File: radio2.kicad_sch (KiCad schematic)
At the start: 18 parts, among them U4 CC1125RHBR, Y1 OW7EL89CENUYO3YLC-40M

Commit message: Finish up inputting things
Signed-off-by: Corey Minyard <corey@minyard.net>
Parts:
- added C49: 39pF, Capacitor_SMD:C_0402_1005Metric_Pad0.74x0.62mm_HandSolder, symbol Device:C
- added C53: 56pF, Capacitor_SMD:C_0402_1005Metric_Pad0.74x0.62mm_HandSolder, symbol Device:C
- added L18: 56nH, Inductor_SMD:L_1210_3225Metric_Pad1.42x2.65mm_HandSolder, symbol Device:L
- added R16: 18, Resistor_SMD:R_0402_1005Metric, symbol Device:R
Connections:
- net 440_TX: now also C49.2; no longer U4.17 (PA)
- new net: C53.1, L18.2, R16.1
- new net: C49.1, L18.1, U4.17 (PA)
- new net +5V: C53.2, R16.2
- no-connect marks 3 -> 5

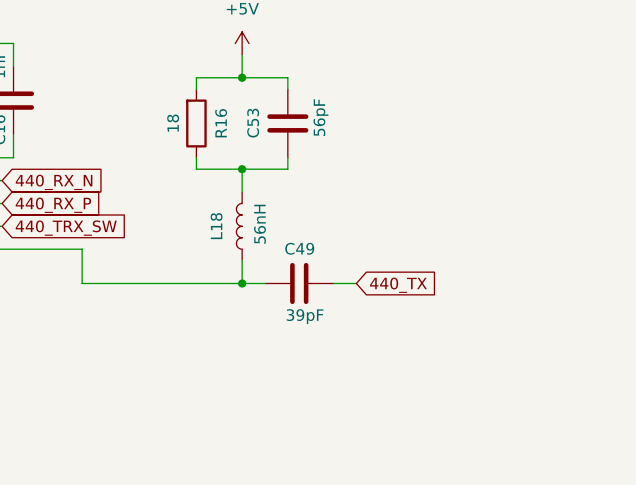
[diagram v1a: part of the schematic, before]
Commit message: Clean up schematics
Signed-off-by: Corey Minyard <corey@minyard.net>
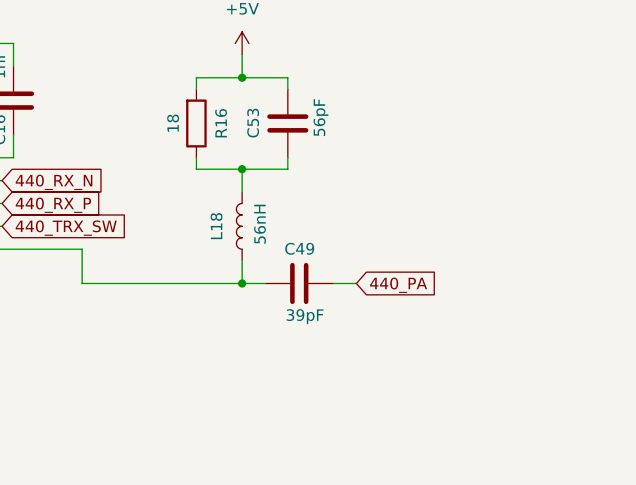
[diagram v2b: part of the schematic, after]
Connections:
- net 440_TX renamed 440_PA
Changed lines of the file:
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@@
 		)
 	)
-	(global_label "440_TX"
+	(global_label "440_PA"
 		(shape input)
 		(at 227.33 119.38 0)
@@
 		)
 		(property "Intersheetrefs" "${INTERSHEET_REFS}"
-			(at 237.0884 119.38 0)
+			(at 237.2699 119.38 0)
 			(effects
 				(font
@@
 		(pin "8"
 		)
-	)
+		(instances
+			(project ""
+				(path "/23e49ab9-97e0-460a-806c-ff6f37958474/cf3ac92b-a340-4acf-be56-0f2a6ee7b165"
+					(reference "U4")
+					(unit 1)
+				)
+			)
+		)
+	)

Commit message: More cleanups and add some test points
Signed-off-by: Corey Minyard <corey@minyard.net>
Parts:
- L18: footprint Inductor_SMD:L_1210_3225Metric_Pad1.42x2.65mm_HandSolder -> Inductor_SMD:L_0603_1608Metric_Pad1.05x0.95mm_HandSolder
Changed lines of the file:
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@@
 			)
 		)
-		(property "Footprint" "Inductor_SMD:L_1210_3225Metric_Pad1.42x2.65mm_HandSolder"
+		(property "Footprint" "Inductor_SMD:L_0603_1608Metric_Pad1.05x0.95mm_HandSolder"
 			(at 214.63 113.03 0)
 			(effects

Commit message: Finish layout
Signed-off-by: Corey Minyard <corey@minyard.net>
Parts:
- C14, C17, C18, C19, C20, C21, C22, C23, C24, C25, C26, C27, C28: footprint Capacitor_SMD:C_0603_1608Metric_Pad1.08x0.95mm_HandSolder -> Capacitor_SMD:C_0402_1005Metric_Pad0.74x0.62mm_HandSolder

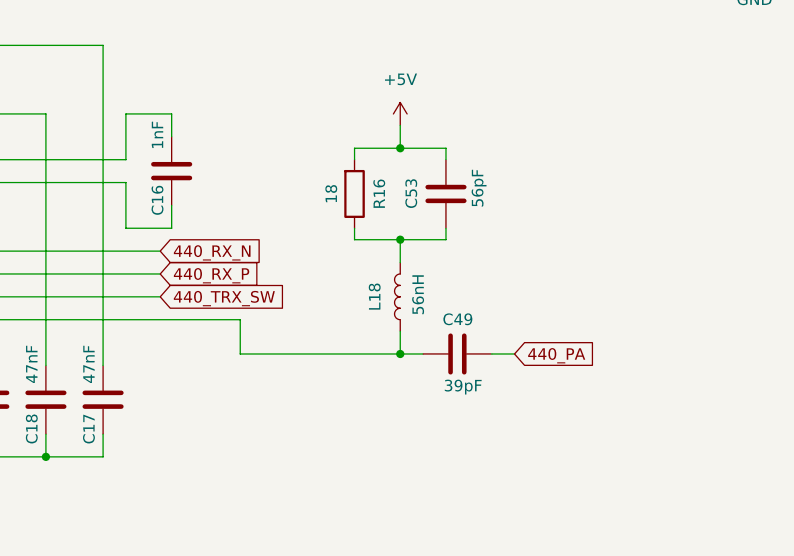
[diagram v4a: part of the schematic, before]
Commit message: Start working on BOM, fix supply indoctors
Signed-off-by: Corey Minyard <corey@minyard.net>
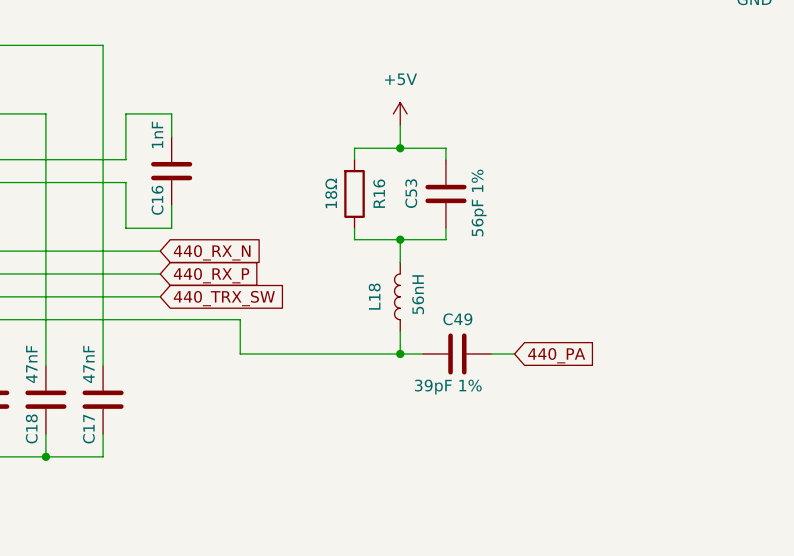
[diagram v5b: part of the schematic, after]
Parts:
- C16: footprint Capacitor_SMD:C_0603_1608Metric_Pad1.08x0.95mm_HandSolder -> Capacitor_SMD:C_0402_1005Metric_Pad0.74x0.62mm_HandSolder
- C49: value 39pF -> 39pF 1%
- C53: value 56pF -> 56pF 1%
- R16: value 18 -> 18Ω
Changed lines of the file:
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@@
 			)
 		)
-		(property "Value" "18"
+		(property "Value" "18Ω"
 			(at 207.01 101.6 90)
 			(effects
@@
 			)
 		)
-		(property "Value" "39pF"
+		(property "Value" "39pF 1%"
 			(at 223.774 122.936 90)
 			(effects
@@
 			)
 		)
-		(property "Value" "56pF"
+		(property "Value" "56pF 1%"
 			(at 223.266 98.806 90)
 			(effects
@@
 			)
 		)
-		(property "Footprint" "Capacitor_SMD:C_0603_1608Metric_Pad1.08x0.95mm_HandSolder"
+		(property "Footprint" "Capacitor_SMD:C_0402_1005Metric_Pad0.74x0.62mm_HandSolder"
 			(at 188.2648 95.25 0)
 			(effects

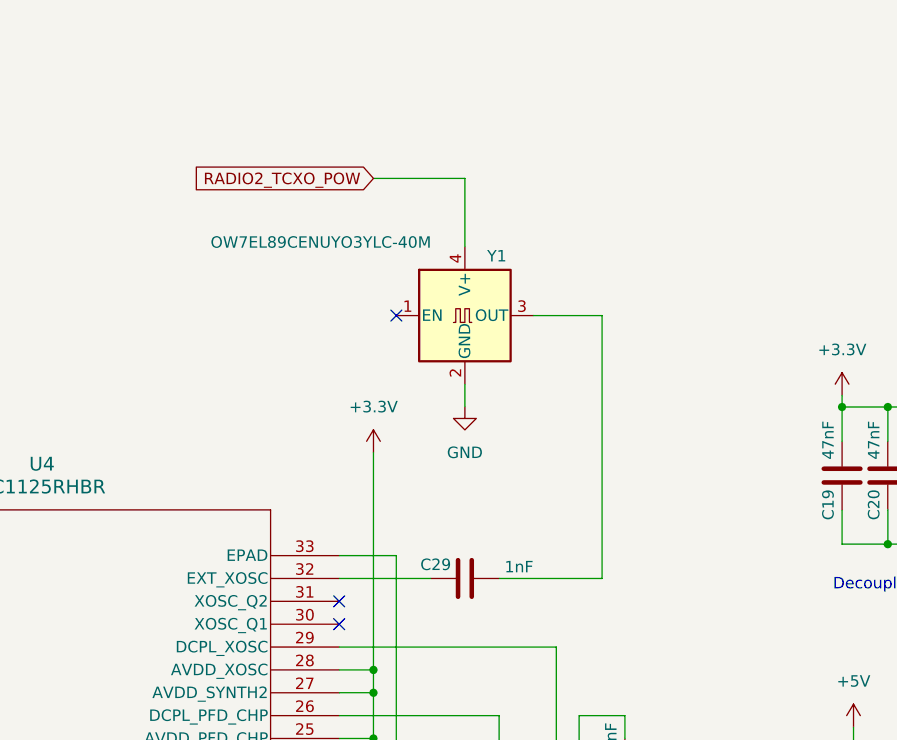
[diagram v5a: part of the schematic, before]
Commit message: Directly power the oscillators
There is only one D/A converter on the CC1312R, so you really couldn't
power both of the oscillators from that chip.  Power is not a concern,
so just directly power them from 3.3V.  That required using a different
oscillator chip, too, but it was available on both frequencies.

Signed-off-by: Corey Minyard <corey@minyard.net>
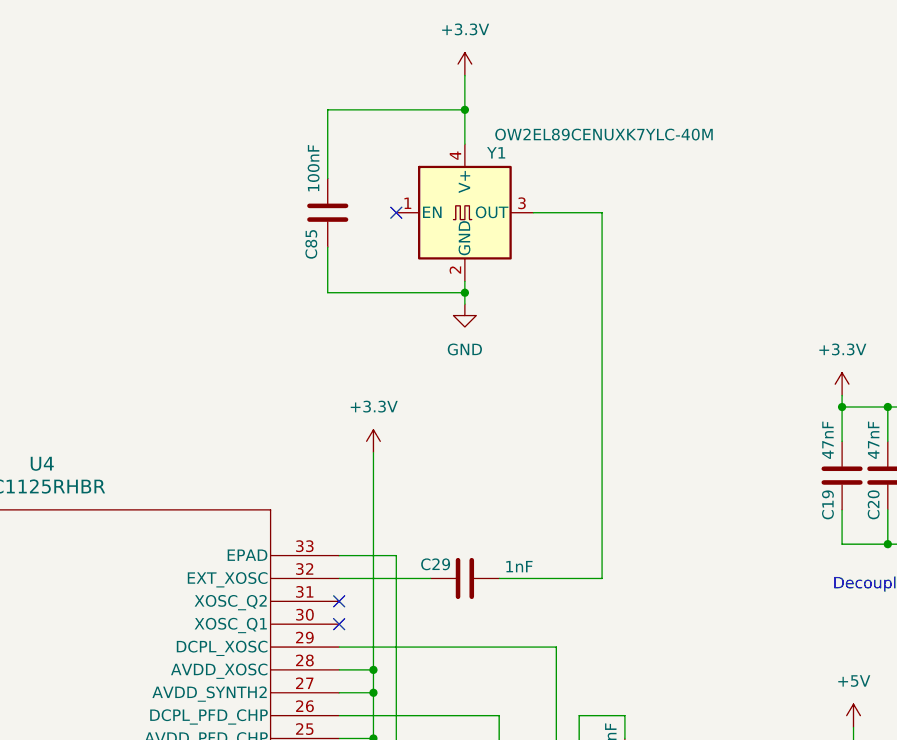
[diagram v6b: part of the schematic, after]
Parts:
- added C85: 100nF, Capacitor_SMD:C_0402_1005Metric_Pad0.74x0.62mm_HandSolder, symbol Device:C
- Y1: value OW7EL89CENUYO3YLC-40M -> OW2EL89CENUXK7YLC-40M
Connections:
- net RADIO2_TCXO_POW is gone; now on net +3.3V: Y1.4 (V+)
- net +3.3V: now also C85.2
- net GND: now also C85.1
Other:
- moved on the sheet: Y1
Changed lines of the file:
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@@
+	)
+	(junction
+		(at 171.45 25.4)
+		(diameter 0)
+		(color 0 0 0 0)
 	)
 	(junction
@@
 		(color 0 0 0 0)
 	)
+	(junction
+		(at 171.45 45.72)
+		(diameter 0)
+		(color 0 0 0 0)
+	)
 	(no_connect
 		(at 157.48 80.01)
@@
 	)
 	(no_connect
-		(at 163.83 48.26)
+		(at 163.83 36.83)
 	)
 	(no_connect
@@
 	(wire
 		(pts
+			(xy 171.45 25.4) (xy 171.45 29.21)
+		)
+		(stroke
+			(width 0)
+			(type default)
+		)
+	)
+	(wire
+		(pts
 			(xy 59.69 90.17) (xy 91.44 90.17)
 		)
@@
 	(wire
 		(pts
-			(xy 171.45 33.02) (xy 171.45 40.64)
+			(xy 171.45 21.59) (xy 171.45 25.4)
 		)
 		(stroke
@@
 	(wire
 		(pts
-			(xy 161.29 33.02) (xy 171.45 33.02)
-		)
-		(stroke
-			(width 0)
-			(type default)
-		)
-	)
-	(wire
-		(pts
 			(xy 243.84 58.42) (xy 248.92 58.42)
 		)
@@
 	(wire
 		(pts
-			(xy 186.69 48.26) (xy 179.07 48.26)
+			(xy 186.69 36.83) (xy 179.07 36.83)
 		)
 		(stroke
@@
 	(wire
 		(pts
-			(xy 171.45 55.88) (xy 171.45 58.42)
+			(xy 171.45 44.45) (xy 171.45 45.72)
 		)
 		(stroke
@@
 	(wire
 		(pts
+			(xy 171.45 45.72) (xy 171.45 46.99)
+		)
+		(stroke
+			(width 0)
+			(type default)
+		)
+	)
+	(wire
+		(pts
 			(xy 157.48 102.87) (xy 161.29 102.87)
 		)
@@
 	(wire
 		(pts
+			(xy 156.21 25.4) (xy 171.45 25.4)
+		)
+		(stroke
+			(width 0)
+			(type default)
+		)
+	)
+	(wire
+		(pts
 			(xy 218.44 58.42) (xy 213.36 58.42)
 		)
@@
 	(wire
 		(pts
-			(xy 186.69 77.47) (xy 186.69 48.26)
+			(xy 186.69 77.47) (xy 186.69 36.83)
 		)
 		(stroke
@@
 	(wire
 		(pts
+			(xy 156.21 45.72) (xy 171.45 45.72)
+		)
+		(stroke
+			(width 0)
+			(type default)
+		)
+	)
+	(wire
+		(pts
 			(xy 87.63 85.09) (xy 87.63 74.93)
 		)
@@
 	(wire
 		(pts
+			(xy 156.21 33.02) (xy 156.21 25.4)
+		)
+		(stroke
+			(width 0)
+			(type default)
+		)
+	)
+	(wire
+		(pts
+			(xy 156.21 40.64) (xy 156.21 45.72)
+		)
+		(stroke
+			(width 0)
+			(type default)
+		)
+	)
+	(wire
+		(pts
 			(xy 157.48 90.17) (xy 161.29 90.17)
 		)
@@
 			(width 0)
 			(type default)
-		)
-	)
-	(global_label "RADIO2_TCXO_POW"
-		(shape input)
-		(at 161.29 33.02 180)
-		(fields_autoplaced yes)
-		(effects
-			(font
-				(size 1.27 1.27)
-			)
-			(justify right)
-		)
-		(property "Intersheetrefs" "${INTERSHEET_REFS}"
-			(at 140.7667 33.02 0)
-			(effects
-				(font
-					(size 1.27 1.27)
-				)
-				(justify right)
-				(hide yes)
-			)
 		)
 	)
@@
 	)
 	(symbol
+		(lib_id "Device:C")
+		(at 156.21 36.83 180)
+		(unit 1)
+		(exclude_from_sim no)
+		(in_bom yes)
+		(on_board yes)
+		(dnp no)
+		(property "Reference" "C85"
+			(at 154.432 38.608 90)
+			(effects
+				(font
+					(size 1.27 1.27)
+				)
+				(justify left)
+			)
+		)
+		(property "Value" "100nF"
+			(at 154.686 29.21 90)
+			(effects
+				(font
+					(size 1.27 1.27)
+				)
+				(justify left)
+			)
+		)
+		(property "Footprint" "Capacitor_SMD:C_0402_1005Metric_Pad0.74x0.62mm_HandSolder"
+			(at 155.2448 33.02 0)
+			(effects
+				(font
+					(size 1.27 1.27)
+				)
+				(hide yes)
+			)
+		)
+		(property "Datasheet" "~"
+			(at 156.21 36.83 0)
+			(effects
+				(font
+					(size 1.27 1.27)
+				)
+				(hide yes)
+			)
+		)
+		(property "Description" "Unpolarized capacitor"
+			(at 156.21 36.83 0)
+			(effects
+				(font
+					(size 1.27 1.27)
+				)
+				(hide yes)
+			)
+		)
+		(pin "2"
+		)
+		(pin "1"
+		)
+		(instances
+			(project "FSKGroundStation"
+				(path "/23e49ab9-97e0-460a-806c-ff6f37958474/cf3ac92b-a340-4acf-be56-0f2a6ee7b165"
+					(reference "C85")
+					(unit 1)
+				)
+			)
+		)
+	)
+	(symbol
 		(lib_id "power:+3.3V")
 		(at 213.36 57.15 0)
@@
 	)
 	(symbol
+		(lib_id "power:+3.3V")
+		(at 171.45 21.59 0)
+		(unit 1)
+		(exclude_from_sim no)
+		(in_bom yes)
+		(on_board yes)
+		(dnp no)
+		(fields_autoplaced yes)
+		(property "Reference" "#PWR096"
+			(at 171.45 25.4 0)
+			(effects
+				(font
+					(size 1.27 1.27)
+				)
+				(hide yes)
+			)
+		)
+		(property "Value" "+3.3V"
+			(at 171.45 16.51 0)
+			(effects
+				(font
+					(size 1.27 1.27)
+				)
+			)
+		)
+		(property "Footprint" ""
+			(at 171.45 21.59 0)
+			(effects
+				(font
+					(size 1.27 1.27)
+				)
+				(hide yes)
+			)
+		)
+		(property "Datasheet" ""
+			(at 171.45 21.59 0)
+			(effects
+				(font
+					(size 1.27 1.27)
+				)
+				(hide yes)
+			)
+		)
+		(property "Description" "Power symbol creates a global label with name \"+3.3V\""
+			(at 171.45 21.59 0)
+			(effects
+				(font
+					(size 1.27 1.27)
+				)
+				(hide yes)
+			)
+		)
+		(pin "1"
+		)
+		(instances
+			(project "FSKGroundStation"
+				(path "/23e49ab9-97e0-460a-806c-ff6f37958474/cf3ac92b-a340-4acf-be56-0f2a6ee7b165"
+					(reference "#PWR096")
+					(unit 1)
+				)
+			)
+		)
+	)
+	(symbol
 		(lib_id "Device:C")
 		(at 223.52 66.04 180)
@@
 	(symbol
 		(lib_id "power:GND")
-		(at 171.45 58.42 0)
+		(at 171.45 46.99 0)
 		(unit 1)
 		(exclude_from_sim no)
@@
 		(fields_autoplaced yes)
 		(property "Reference" "#PWR031"
-			(at 171.45 64.77 0)
+			(at 171.45 53.34 0)
 			(effects
 				(font
@@
 		)
 		(property "Value" "GND"
-			(at 171.45 63.5 0)
+			(at 171.45 52.07 0)
 			(effects
 				(font
@@
 		)
 		(property "Footprint" ""
-			(at 171.45 58.42 0)
+			(at 171.45 46.99 0)
 			(effects
 				(font
@@
 		)
 		(property "Datasheet" ""
-			(at 171.45 58.42 0)
+			(at 171.45 46.99 0)
 			(effects
 				(font
@@
 		)
 		(property "Description" "Power symbol creates a global label with name \"GND\" , ground"
-			(at 171.45 58.42 0)
+			(at 171.45 46.99 0)
 			(effects
 				(font
@@
 	(symbol
 		(lib_id "Local Passives:TXCO")
-		(at 171.45 48.26 0)
+		(at 171.45 36.83 0)
 		(unit 1)
 		(exclude_from_sim no)
@@
 		(dnp no)
 		(property "Reference" "Y1"
-			(at 175.006 41.656 0)
-			(effects
-				(font
-					(size 1.27 1.27)
-				)
-			)
-		)
-		(property "Value" "OW7EL89CENUYO3YLC-40M"
-			(at 155.448 40.132 0)
+			(at 175.006 30.226 0)
+			(effects
+				(font
+					(size 1.27 1.27)
+				)
+			)
+		)
+		(property "Value" "OW2EL89CENUXK7YLC-40M"
+			(at 186.944 28.194 0)
 			(effects
 				(font
@@
 		)
 		(property "Footprint" "Oscillator:Oscillator_SMD_SiT_PQFN-4Pin_2.0x1.6mm"
-			(at 189.23 57.15 0)
+			(at 189.23 45.72 0)
 			(effects
 				(font
@@
 		)
 		(property "Datasheet" ""
-			(at 168.91 48.26 0)
+			(at 168.91 36.83 0)
 			(effects
 				(font
@@
 		)
 		(property "Description" "TXCO 2.0mmx1.6mm"
-			(at 171.45 48.26 0)
-			(effects
-				(font
+			(at 171.45 36.83 0)
+			(effects
+				(font

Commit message: Fix some oscillator issues
Ground an unused oscillator line on the CC1125 that needs to be grounded
in external oscillator mode.

Add a resistor divider to the oscillator inputs in case the voltage
needs to be decreased.  It should be fixable with the internal capacitor
tuning, but just in case.

Signed-off-by: Corey Minyard <corey@minyard.net>
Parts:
- added R14, R31: 0Ω, Resistor_SMD:R_0402_1005Metric, symbol Device:R
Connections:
- net GND: now also U4.30 (XOSC_Q1), R31.1
- net at Y1.3 (OUT): now also R14.2; no longer C29.2
- new net: C29.2, R14.1, R31.2
- no-connect marks 5 -> 4
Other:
- note added: "This is in case we need to reduce the voltage into the oscillator pin."

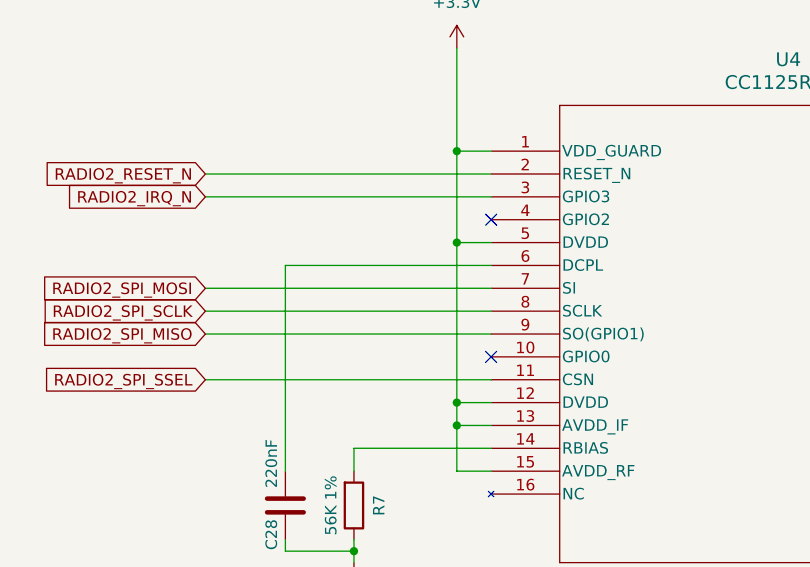
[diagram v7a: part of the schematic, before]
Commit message: Make a bunch of GPIOs more easily available
Put them on DNP zero-ohm resistors.

Signed-off-by: Corey Minyard <corey@minyard.net>
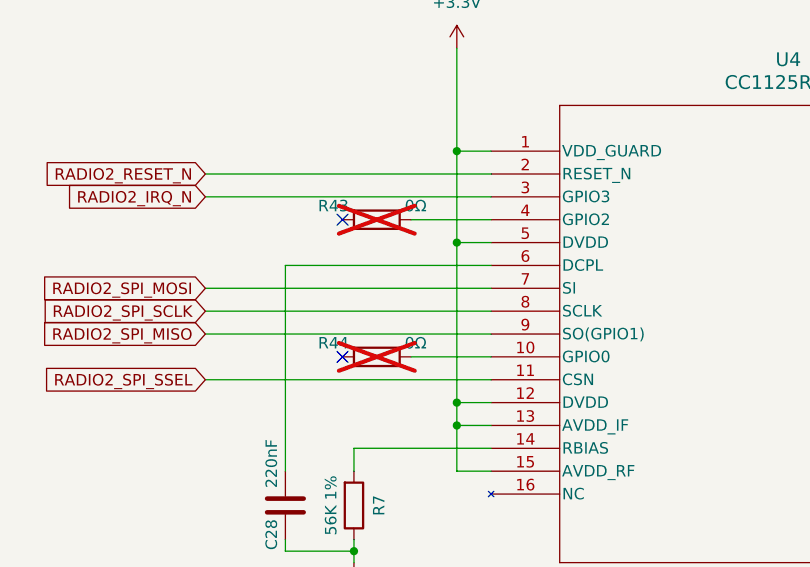
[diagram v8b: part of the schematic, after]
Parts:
- added R43, R44: 0Ω, Resistor_SMD:R_0402_1005Metric, symbol Device:R
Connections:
- net at U4.10 (GPIO0): now also R44.1
- net at U4.4 (GPIO2): now also R43.1
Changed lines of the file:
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@@
 	)
 	(no_connect
-		(at 91.44 97.79)
+		(at 74.93 82.55)
+	)
+	(no_connect
+		(at 74.93 97.79)
 	)
 	(no_connect
 		(at 163.83 36.83)
 	)
-	(no_connect
-		(at 91.44 82.55)
-	)
 	(wire
 		(pts
@@
 	(wire
 		(pts
+			(xy 82.55 97.79) (xy 91.44 97.79)
+		)
+		(stroke
+			(width 0)
+			(type default)
+		)
+	)
+	(wire
+		(pts
 			(xy 189.23 102.87) (xy 189.23 105.41)
 		)
@@
 		(pts
 			(xy 87.63 110.49) (xy 87.63 105.41)
+		)
+		(stroke
+			(width 0)
+			(type default)
+		)
+	)
+	(wire
+		(pts
+			(xy 82.55 82.55) (xy 91.44 82.55)
 		)
 		(stroke
@@
 	)
 	(symbol
+		(lib_id "Device:R")
+		(at 78.74 82.55 270)
+		(unit 1)
+		(exclude_from_sim no)
+		(in_bom no)
+		(on_board yes)
+		(dnp yes)
+		(property "Reference" "R43"
+			(at 73.914 81.026 90)
+			(effects
+				(font
+					(size 1.27 1.27)
+				)
+			)
+		)
+		(property "Value" "0Ω"
+			(at 83.058 81.026 90)
+			(effects
+				(font
+					(size 1.27 1.27)
+				)
+			)
+		)
+		(property "Footprint" "Resistor_SMD:R_0402_1005Metric"
+			(at 78.74 80.772 90)
+			(effects
+				(font
+					(size 1.27 1.27)
+				)
+				(hide yes)
+			)
+		)
+		(property "Datasheet" "~"
+			(at 78.74 82.55 0)
+			(effects
+				(font
+					(size 1.27 1.27)
+				)
+				(hide yes)
+			)
+		)
+		(property "Description" "Resistor"
+			(at 78.74 82.55 0)
+			(effects
+				(font
+					(size 1.27 1.27)
+				)
+				(hide yes)
+			)
+		)
+		(pin "2"
+		)
+		(pin "1"
+		)
+		(instances
+			(project "FSKGroundStation"
+				(path "/23e49ab9-97e0-460a-806c-ff6f37958474/cf3ac92b-a340-4acf-be56-0f2a6ee7b165"
+					(reference "R43")
+					(unit 1)
+				)
+			)
+		)
+	)
+	(symbol
 		(lib_id "power:GND")
 		(at 191.77 59.69 0)
@@
 					(unit 1)
 				)
+			)
+		)
+	)
+	(symbol
+		(lib_id "Device:R")
+		(at 78.74 97.79 270)
+		(unit 1)
+		(exclude_from_sim no)
+		(in_bom no)
+		(on_board yes)
+		(dnp yes)
+		(property "Reference" "R44"
+			(at 73.914 96.266 90)
+			(effects
+				(font
+					(size 1.27 1.27)
+				)
+			)
+		)
+		(property "Value" "0Ω"
+			(at 83.058 96.266 90)
+			(effects
+				(font
+					(size 1.27 1.27)
+				)
+			)
+		)
+		(property "Footprint" "Resistor_SMD:R_0402_1005Metric"
+			(at 78.74 96.012 90)
+			(effects
+				(font
+					(size 1.27 1.27)
+				)
+				(hide yes)
+			)
+		)
+		(property "Datasheet" "~"
+			(at 78.74 97.79 0)
+			(effects
+				(font
+					(size 1.27 1.27)
+				)
+				(hide yes)
+			)
+		)
+		(property "Description" "Resistor"
+			(at 78.74 97.79 0)
+			(effects
+				(font
+					(size 1.27 1.27)
+				)
+				(hide yes)
+			)
+		)
+		(pin "2"
+		)
+		(pin "1"
+		)
+		(instances
+			(project "FSKGroundStation"
+				(path "/23e49ab9-97e0-460a-806c-ff6f37958474/cf3ac92b-a340-4acf-be56-0f2a6ee7b165"
+					(reference "R44")
+					(unit 1)
+				)
